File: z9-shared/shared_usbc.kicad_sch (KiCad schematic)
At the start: 10 parts, among them J801 USB_C_Receptacle_USB2.0_16P

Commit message: pre kicad update
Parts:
- renumbered C801 to C?, D801 to D?, D802 to D?, F801 to F?, J801 to J?, R805 to R?, R801 to R?, R802 to R?, R804 to R?, R803 to R?
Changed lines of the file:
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@@
 		(on_board yes)
 		(dnp no)
-		(property "Reference" "D801"
+		(property "Reference" "D?"
 			(at 129.032 114.4016 0)
 			(effects
@@
 		(dnp no)
 		(fields_autoplaced yes)
-		(property "Reference" "F801"
+		(property "Reference" "F?"
 			(at 102.87 72.39 90)
 			(effects
@@
 		(on_board yes)
 		(dnp no)
-		(property "Reference" "#PWR0107"
+		(property "Reference" "#PWR0111"
 			(at 62.23 137.16 0)
 			(effects
@@
 		(on_board yes)
 		(dnp no)
-		(property "Reference" "R805"
+		(property "Reference" "R?"
 			(at 182.372 115.57 0)
 			(effects
@@
 		(on_board yes)
 		(dnp no)
-		(property "Reference" "#PWR0104"
+		(property "Reference" "#PWR0108"
 			(at 184.15 137.16 0)
 			(effects
@@
 		(on_board yes)
 		(dnp no)
-		(property "Reference" "#PWR0108"
+		(property "Reference" "#PWR0112"
 			(at 71.12 137.16 0)
 			(effects
@@
 		(on_board yes)
 		(dnp no)
-		(property "Reference" "R801"
+		(property "Reference" "R?"
 			(at 60.198 128.27 90)
 			(effects
@@
 		(on_board yes)
 		(dnp no)
-		(property "Reference" "R802"
+		(property "Reference" "R?"
 			(at 156.718 115.57 0)
 			(effects
@@
 		(on_board yes)
 		(dnp no)
-		(property "Reference" "R804"
+		(property "Reference" "R?"
 			(at 177.8 76.708 90)
 			(effects
@@
 		(dnp no)
 		(fields_autoplaced yes)
-		(property "Reference" "D802"
+		(property "Reference" "D?"
 			(at 167.64 58.1024 0)
 			(effects
@@
 		(dnp no)
 		(fields_autoplaced yes)
-		(property "Reference" "#PWR0102"
+		(property "Reference" "#PWR0106"
 			(at 165.1 54.61 0)
 			(effects
@@
 		(on_board yes)
 		(dnp no)
-		(property "Reference" "#PWR0106"
+		(property "Reference" "#PWR0110"
 			(at 120.65 137.16 0)
 			(effects
@@
 		(on_board yes)
 		(dnp no)
-		(property "Reference" "R803"
+		(property "Reference" "R?"
 			(at 166.878 115.57 0)
 			(effects
@@
 		(dnp no)
 		(fields_autoplaced yes)
-		(property "Reference" "J801"
+		(property "Reference" "J?"
 			(at 78.74 71.12 0)
 			(effects
@@
 		(dnp no)
 		(fields_autoplaced yes)
-		(property "Reference" "#PWR0105"
+		(property "Reference" "#PWR0109"
 			(at 165.1 143.51 0)
 			(effects
@@
 		(dnp no)
 		(fields_autoplaced yes)
-		(property "Reference" "#PWR0103"
+		(property "Reference" "#PWR0107"
 			(at 154.94 143.51 0)
 			(effects
@@
 		(on_board yes)
 		(dnp no)
-		(property "Reference" "C801"
+		(property "Reference" "C?"
 			(at 72.39 128.27 90)
 			(effects
@@
 		(on_board yes)
 		(dnp no)
-		(property "Reference" "#PWR0109"
+		(property "Reference" "#PWR0113"
 			(at 78.74 137.16 0)
 			(effects

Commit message: x
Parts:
- gave numbers to parts that had none: 10
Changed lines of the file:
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@@
 		(on_board yes)
 		(dnp no)
-		(property "Reference" "D?"
+		(property "Reference" "D801"
 			(at 129.032 114.4016 0)
 			(effects
@@
 		(dnp no)
 		(fields_autoplaced yes)
-		(property "Reference" "F?"
+		(property "Reference" "F801"
 			(at 102.87 72.39 90)
 			(effects
@@
 		(on_board yes)
 		(dnp no)
-		(property "Reference" "#PWR0111"
+		(property "Reference" "#PWR0107"
 			(at 62.23 137.16 0)
 			(effects
@@
 		(on_board yes)
 		(dnp no)
-		(property "Reference" "R?"
+		(property "Reference" "R805"
 			(at 182.372 115.57 0)
 			(effects
@@
 		(on_board yes)
 		(dnp no)
-		(property "Reference" "#PWR0108"
+		(property "Reference" "#PWR0104"
 			(at 184.15 137.16 0)
 			(effects
@@
 		(on_board yes)
 		(dnp no)
-		(property "Reference" "#PWR0112"
+		(property "Reference" "#PWR0108"
 			(at 71.12 137.16 0)
 			(effects
@@
 		(on_board yes)
 		(dnp no)
-		(property "Reference" "R?"
+		(property "Reference" "R801"
 			(at 60.198 128.27 90)
 			(effects
@@
 		(on_board yes)
 		(dnp no)
-		(property "Reference" "R?"
+		(property "Reference" "R802"
 			(at 156.718 115.57 0)
 			(effects
@@
 		(on_board yes)
 		(dnp no)
-		(property "Reference" "R?"
+		(property "Reference" "R804"
 			(at 177.8 76.708 90)
 			(effects
@@
 		(dnp no)
 		(fields_autoplaced yes)
-		(property "Reference" "D?"
+		(property "Reference" "D802"
 			(at 167.64 58.1024 0)
 			(effects
@@
 		(dnp no)
 		(fields_autoplaced yes)
-		(property "Reference" "#PWR0106"
+		(property "Reference" "#PWR0102"
 			(at 165.1 54.61 0)
 			(effects
@@
 		(on_board yes)
 		(dnp no)
-		(property "Reference" "#PWR0110"
+		(property "Reference" "#PWR0106"
 			(at 120.65 137.16 0)
 			(effects
@@
 		(on_board yes)
 		(dnp no)
-		(property "Reference" "R?"
+		(property "Reference" "R803"
 			(at 166.878 115.57 0)
 			(effects
@@
 		(dnp no)
 		(fields_autoplaced yes)
-		(property "Reference" "J?"
+		(property "Reference" "J801"
 			(at 78.74 71.12 0)
 			(effects
@@
 		(dnp no)
 		(fields_autoplaced yes)
-		(property "Reference" "#PWR0109"
+		(property "Reference" "#PWR0105"
 			(at 165.1 143.51 0)
 			(effects
@@
 		(dnp no)
 		(fields_autoplaced yes)
-		(property "Reference" "#PWR0107"
+		(property "Reference" "#PWR0103"
 			(at 154.94 143.51 0)
 			(effects
@@
 		(on_board yes)
 		(dnp no)
-		(property "Reference" "C?"
+		(property "Reference" "C801"
 			(at 72.39 128.27 90)
 			(effects
@@
 		(on_board yes)
 		(dnp no)
-		(property "Reference" "#PWR0113"
+		(property "Reference" "#PWR0109"
 			(at 78.74 137.16 0)
 			(effects

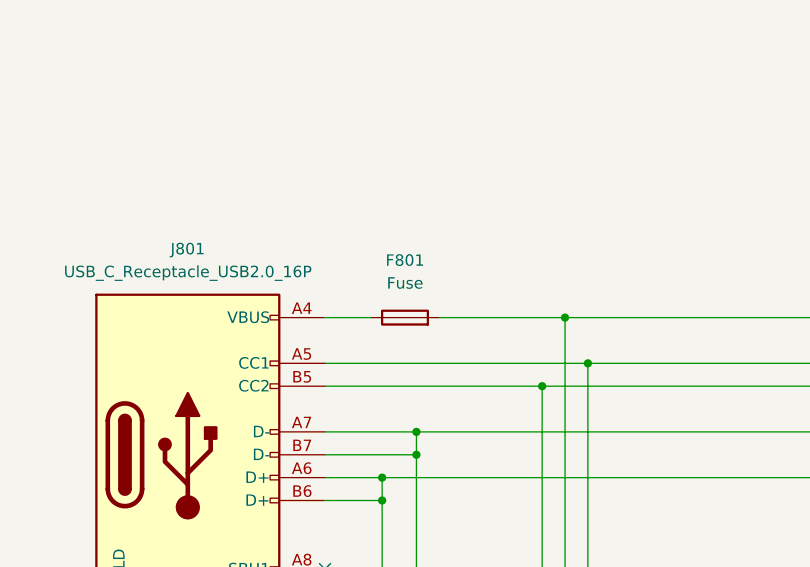
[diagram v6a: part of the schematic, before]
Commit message: new fuse and ideal diode
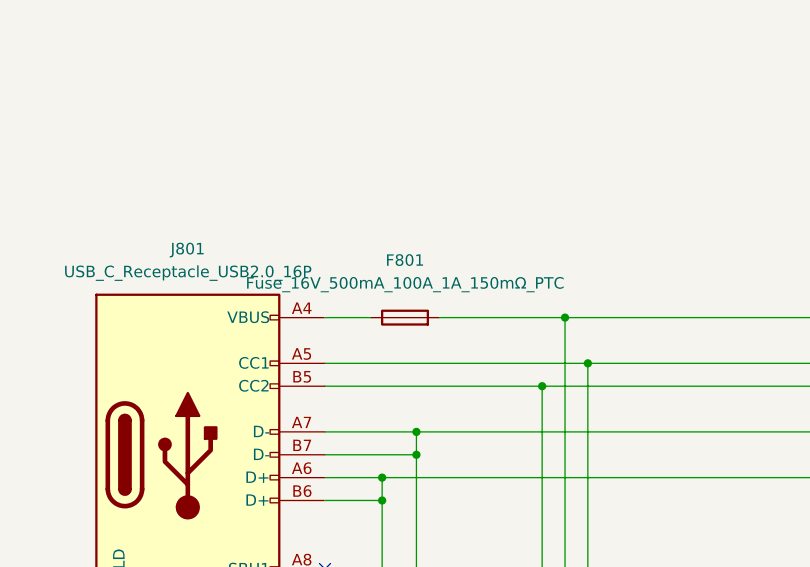
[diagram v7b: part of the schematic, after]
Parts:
- F801: value Fuse -> Fuse_16V_500mA_100A_1A_150mΩ_PTC
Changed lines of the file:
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@@
 			)
 		)
-		(property "Value" "Fuse"
+		(property "Value" "Fuse_16V_500mA_100A_1A_150mΩ_PTC"
 			(at 102.87 74.93 90)
 			(effects
@@
 			(effects
 				(font
-					(size 1.27 1.27)
-				)
-				(hide yes)
-			)
-		)
-		(property "Order" ""
-			(at 102.87 78.74 90)
-			(effects
-				(font
-					(size 1.27 1.27)
-				)
-				(hide yes)
-			)
-		)
-		(property "PN" ""
-			(at 102.87 78.74 90)
-			(effects
-				(font
-					(size 1.27 1.27)
-				)
-				(hide yes)
-			)
-		)
-		(property "Part Number" ""
-			(at 102.87 78.74 90)
-			(effects
-				(font
-					(size 1.27 1.27)
-				)
-				(hide yes)
-			)
-		)
-		(property "Part#" ""
-			(at 102.87 78.74 90)
-			(effects
-				(font
-					(size 1.27 1.27)
-				)
-				(hide yes)
-			)
-		)
-		(property "Vendor" ""
-			(at 102.87 78.74 90)
-			(effects
-				(font
-					(size 1.27 1.27)
-				)
-				(hide yes)
-			)
-		)
-		(property "Voltage" ""
-			(at 102.87 78.74 90)
-			(effects
-				(font

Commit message: x
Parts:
- J18: renamed from J801; footprint Connector_USB:USB_C_Receptacle_G-Switch_GT-USB-7051x -> dnt:USB_C_Receptacle_G-Switch_GT-USB-7051x
- renumbered C801 to C55, D801 to D33, D802 to D34, F801 to F9, R801 to R71, R802 to R72, R803 to R73, R804 to R74, R805 to R75
